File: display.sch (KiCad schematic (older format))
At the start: 1 part

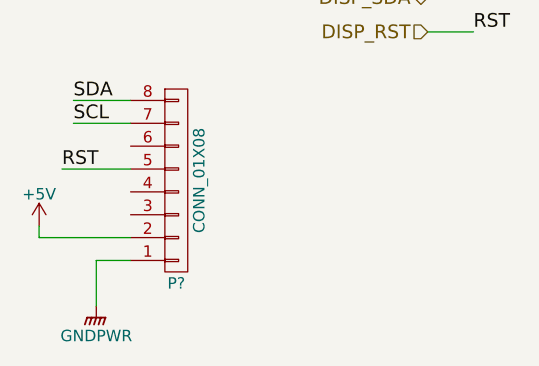
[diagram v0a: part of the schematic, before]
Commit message: added component values and most packages. Still missing micro usb
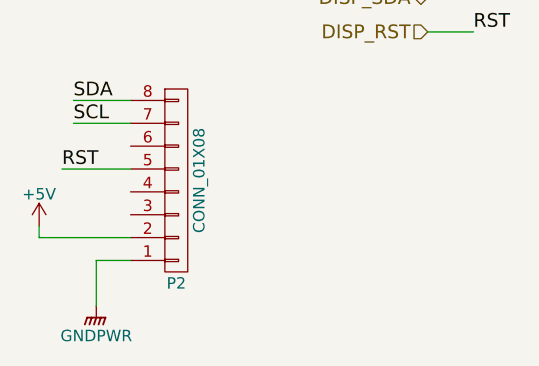
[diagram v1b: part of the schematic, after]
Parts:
- P2: renamed from P?; footprint (none) -> Pin_Headers:Pin_Header_Straight_1x08
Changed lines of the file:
@@
 $EndDescr
 $Comp
-L CONN_01X08 P?
+L CONN_01X08 P2
 U 1 1 564032DD
 P 4850 3050
-F 0 "P?" H 4850 3500 50  0000 C CNN
+F 0 "P2" H 4850 3500 50  0000 C CNN
 F 1 "CONN_01X08" V 4950 3050 50  0000 C CNN
-F 2 "" H 4850 3050 60  0000 C CNN
+F 2 "Pin_Headers:Pin_Header_Straight_1x08" H 4850 3050 60  0001 C CNN
 F 3 "" H 4850 3050 60  0000 C CNN
 	1    4850 3050
@@
 $EndComp
 $Comp
-L +5V #PWR?
+L +5V #PWR024
 U 1 1 56403310
 P 4250 3250
-F 0 "#PWR?" H 4250 3100 50  0001 C CNN
+F 0 "#PWR024" H 4250 3100 50  0001 C CNN
 F 1 "+5V" H 4250 3390 50  0000 C CNN
 F 2 "" H 4250 3250 60  0000 C CNN
@@
 $EndComp
 $Comp
-L GNDPWR #PWR?
+L GNDPWR #PWR025
 U 1 1 56403326
 P 4500 3600
-F 0 "#PWR?" H 4500 3400 50  0001 C CNN
+F 0 "#PWR025" H 4500 3400 50  0001 C CNN
 F 1 "GNDPWR" H 4500 3470 50  0000 C CNN
 F 2 "" H 4500 3550 60  0000 C CNN

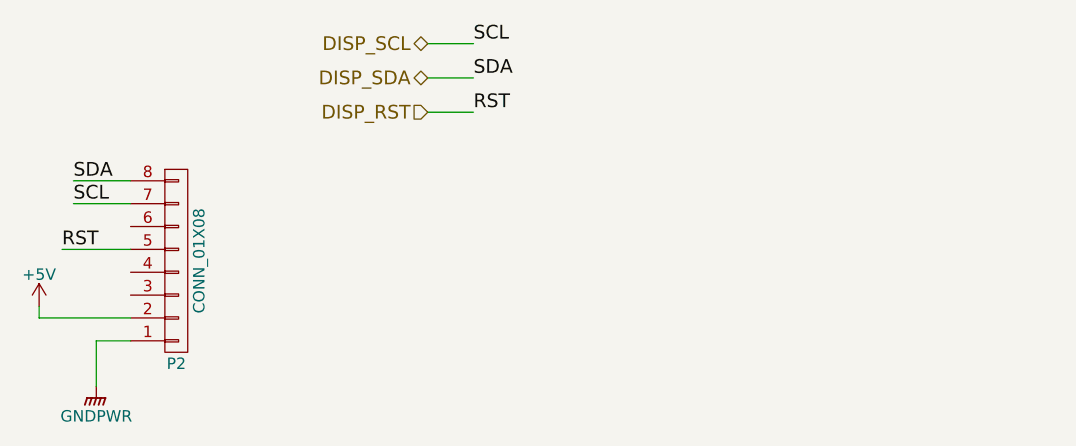
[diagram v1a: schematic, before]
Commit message: Added a USB socket with GND set as a power output to pass DRC, and gave a first stab at a placement. Man that's tight! Components both side required??
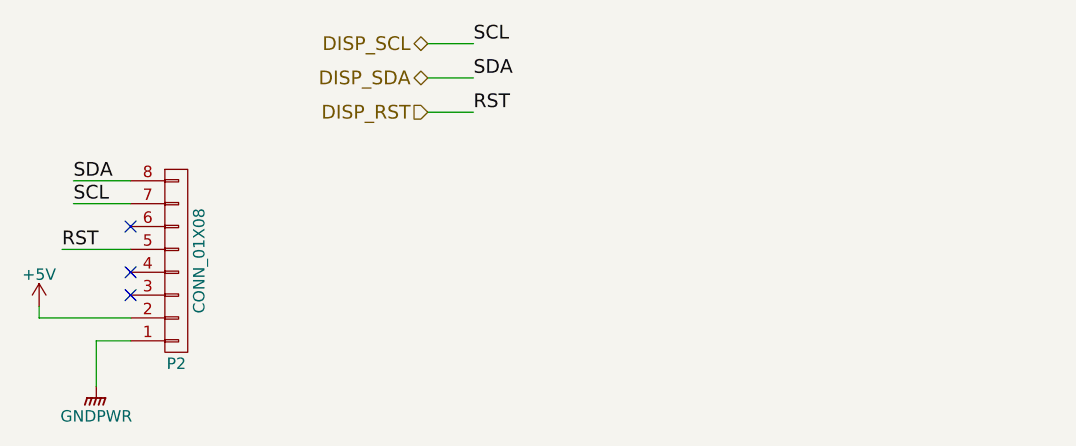
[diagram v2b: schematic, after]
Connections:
- no-connect marks 0 -> 3
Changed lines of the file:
@@
 Wire Wire Line
 	5950 2400 6150 2400
+NoConn ~ 4650 2900
+NoConn ~ 4650 3100
+NoConn ~ 4650 3200
 $EndSCHEMATC

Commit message: Dodgy layout added, etc
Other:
- note added: "Note, pullups are fitted on display module, 10k to 3V3"
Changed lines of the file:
@@
 EESchema Schematic File Version 2
+LIBS:weatherstation-rescue
 LIBS:power
 LIBS:device
@@
 NoConn ~ 4650 3100
 NoConn ~ 4650 3200
+Text Notes 5600 3000 0    60   ~ 0
+Note, pullups are fitted on display module, 10k to 3V3
 $EndSCHEMATC
